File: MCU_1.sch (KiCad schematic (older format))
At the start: 18 parts, among them U2 STM32F051K6Ux

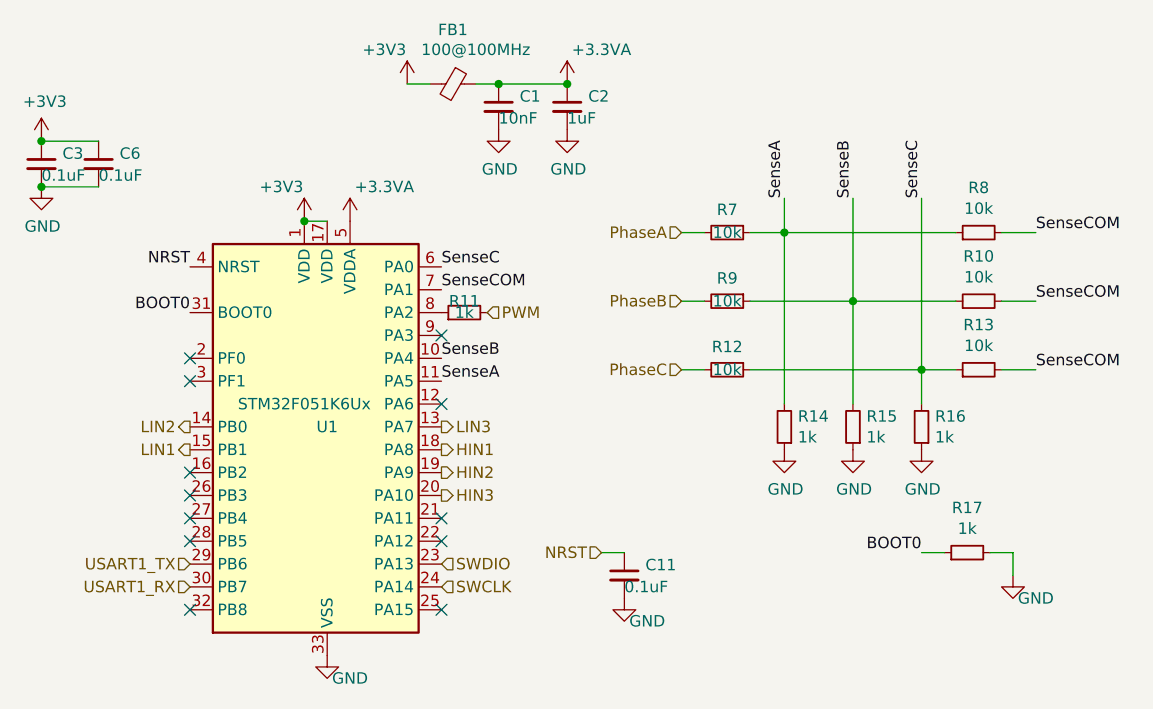
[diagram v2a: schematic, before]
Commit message: Rerouted a bunch of the phase traces so they are shorter
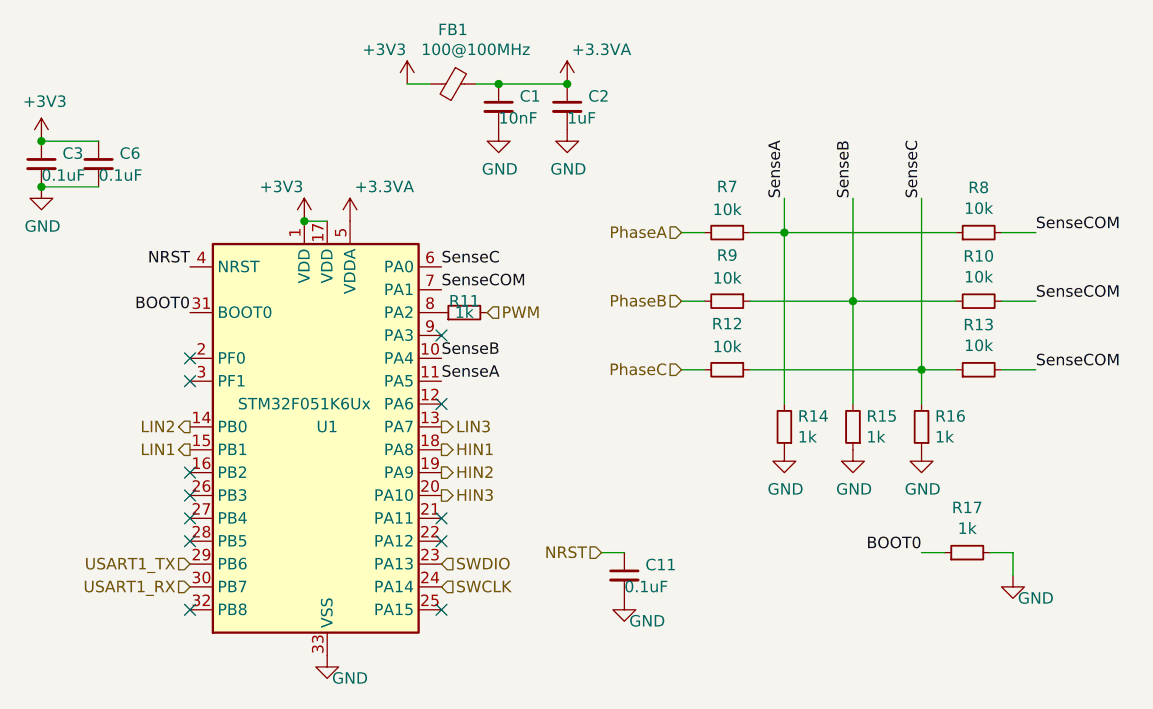
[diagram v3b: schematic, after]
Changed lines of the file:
@@
 AR Path="/6054D32F/6050F9A3" Ref="R7"  Part="1"
 AR Path="/605CA831/6050F9A3" Ref="R38"  Part="1"
-F 0 "R7" V 6700 2100 50  0000 C CNN
-F 1 "10k" V 6800 2100 50  0000 C CNN
+F 0 "R7" V 6600 2100 50  0000 C CNN
+F 1 "10k" V 6700 2100 50  0000 C CNN
 F 2 "Resistor_SMD:R_0402_1005Metric" H 6800 2100 50  0001 C CNN
 F 3 "~" H 6800 2100 50  0001 C CNN
@@
 AR Path="/6054D32F/6038A448" Ref="R9"  Part="1"
 AR Path="/605CA831/6038A448" Ref="R40"  Part="1"
-F 0 "R9" V 6700 2400 50  0000 C CNN
-F 1 "10k" V 6800 2400 50  0000 C CNN
+F 0 "R9" V 6600 2400 50  0000 C CNN
+F 1 "10k" V 6700 2400 50  0000 C CNN
 F 2 "Resistor_SMD:R_0402_1005Metric" H 6800 2400 50  0001 C CNN
 F 3 "~" H 6800 2400 50  0001 C CNN
@@
 AR Path="/6054D32F/6038D85A" Ref="R12"  Part="1"
 AR Path="/605CA831/6038D85A" Ref="R43"  Part="1"
-F 0 "R12" V 6700 2700 50  0000 C CNN
-F 1 "10k" V 6800 2700 50  0000 C CNN
+F 0 "R12" V 6600 2700 50  0000 C CNN
+F 1 "10k" V 6700 2700 50  0000 C CNN
 F 2 "Resistor_SMD:R_0402_1005Metric" H 6800 2700 50  0001 C CNN
 F 3 "~" H 6800 2700 50  0001 C CNN

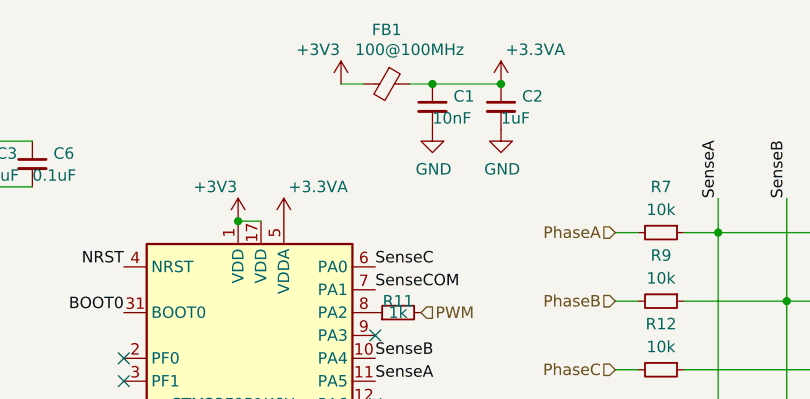
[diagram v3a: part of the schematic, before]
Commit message: Finished all traces and vias
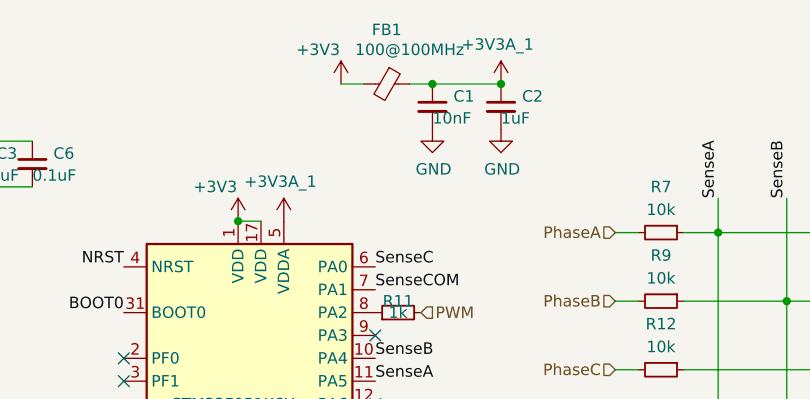
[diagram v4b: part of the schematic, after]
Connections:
- net +3.3VA renamed +3.3VA_1
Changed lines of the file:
@@
 NRST
-$Comp
-L power:+3.3VA #PWR0109
-U 1 1 604543F5
-P 5150 2050
-AR Path="/60302A40/604543F5" Ref="#PWR0109"  Part="1"
-AR Path="/605793E5/604543F5" Ref="#PWR?"  Part="1"
-AR Path="/6054D32F/604543F5" Ref="#PWR0127"  Part="1"
-AR Path="/605CA831/604543F5" Ref="#PWR0187"  Part="1"
-F 0 "#PWR0127" H 5150 1900 50  0001 C CNN
-F 1 "+3.3VA" H 5300 2200 50  0000 C CNN
-F 2 "" H 5150 2050 50  0001 C CNN
-F 3 "" H 5150 2050 50  0001 C CNN
-	1    5150 2050
-	1    0    0    -1
-$EndComp
 $Comp
 L power:+3V3 #PWR0110
@@
 F 3 "" H 5400 1450 50  0001 C CNN
 	1    5400 1450
-	1    0    0    -1
-$EndComp
-$Comp
-L power:+3.3VA #PWR0111
-U 1 1 6050F9B6
-P 6100 1450
-AR Path="/60302A40/6050F9B6" Ref="#PWR0111"  Part="1"
-AR Path="/605793E5/6050F9B6" Ref="#PWR?"  Part="1"
-AR Path="/6054D32F/6050F9B6" Ref="#PWR0162"  Part="1"
-AR Path="/605CA831/6050F9B6" Ref="#PWR0189"  Part="1"
-F 0 "#PWR0162" H 6100 1300 50  0001 C CNN
-F 1 "+3.3VA" H 6250 1600 50  0000 C CNN
-F 2 "" H 6100 1450 50  0001 C CNN
-F 3 "" H 6100 1450 50  0001 C CNN
-	1    6100 1450
 	1    0    0    -1
 $EndComp
@@
 Wire Wire Line
 	5700 1450 5800 1450
-Connection ~ 6100 1450
 Wire Wire Line
 	5800 1450 6100 1450
@@
 Text HLabel 4450 3550 0    50   Input ~ 0
 USART1_TX
+$Comp
+L power:+3V3A_1 #PWR0127
+U 1 1 6056120C
+P 5150 2050
+F 0 "#PWR0127" H 5150 1950 50  0001 C CNN
+F 1 "+3V3A_1" H 5135 2223 50  0000 C CNN
+F 2 "" H 5150 2050 50  0001 C CNN
+F 3 "" H 5150 2050 50  0001 C CNN
+	1    5150 2050
+	1    0    0    -1
+$EndComp
+$Comp
+L power:+3V3A_1 #PWR?
+U 1 1 6056DE0B
+P 6100 1450
+F 0 "#PWR?" H 6100 1350 50  0001 C CNN
+F 1 "+3V3A_1" H 6085 1623 50  0000 C CNN
+F 2 "" H 6100 1450 50  0001 C CNN
+F 3 "" H 6100 1450 50  0001 C CNN
+	1    6100 1450
+	1    0    0    -1
+$EndComp
+Connection ~ 6100 1450
 $EndSCHEMATC

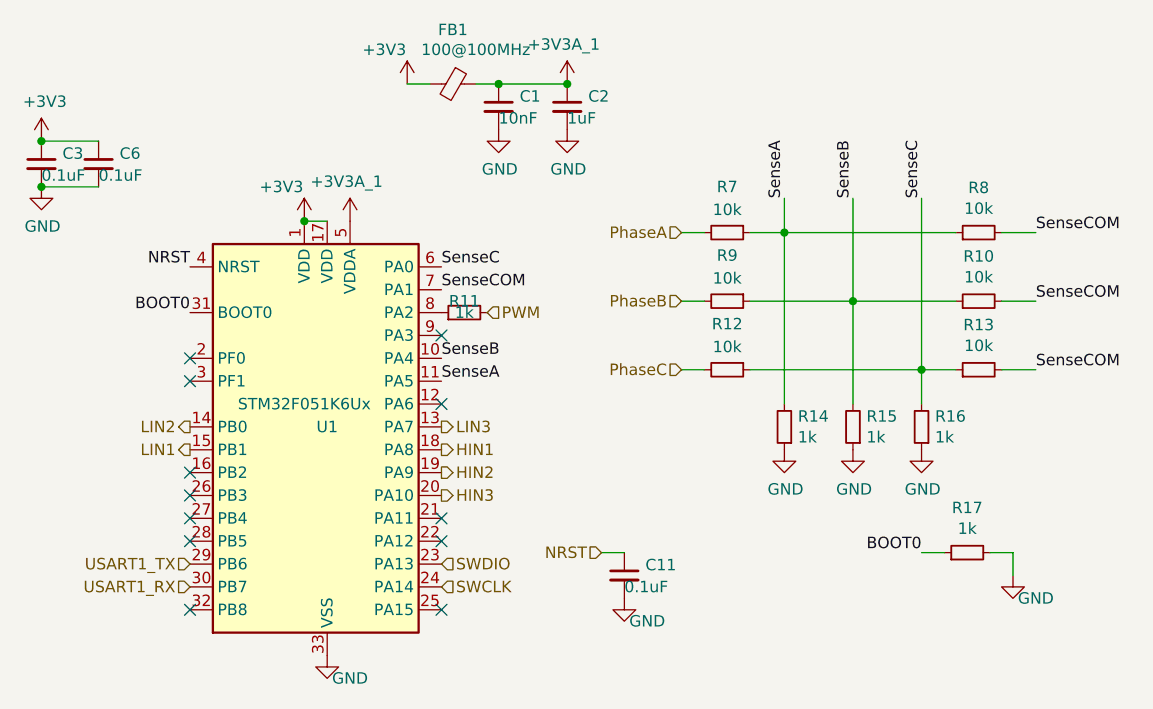
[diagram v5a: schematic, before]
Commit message: Changed shunt resistor footprint and changed edge cuts to accomodate larger size
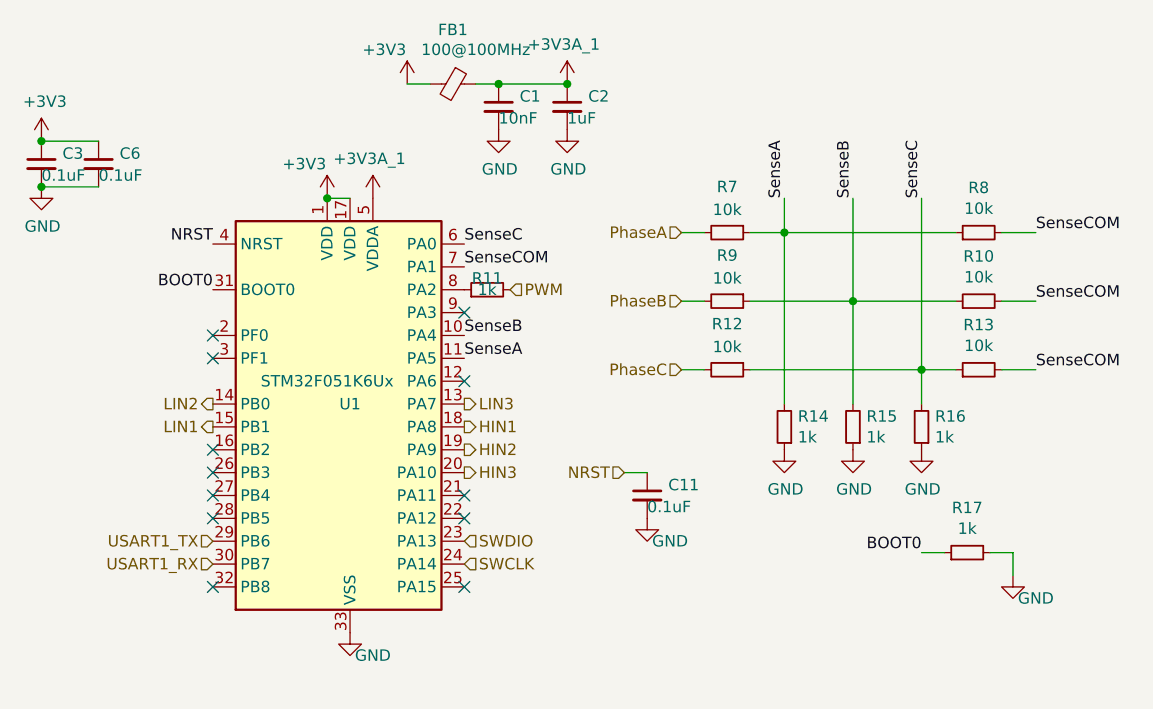
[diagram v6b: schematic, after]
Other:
- moved on the sheet: C11, R11, U1
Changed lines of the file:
@@
 L MCU_ST_STM32F0:STM32F051K6Ux U2
 U 1 1 60305B87
-P 5050 2950
+P 5150 2850
 AR Path="/60302A40/60305B87" Ref="U2"  Part="1"
 AR Path="/605793E5/60305B87" Ref="U?"  Part="1"
 AR Path="/6054D32F/60305B87" Ref="U1"  Part="1"
 AR Path="/605CA831/60305B87" Ref="U9"  Part="1"
-F 0 "U1" H 5050 2950 50  0000 C CNN
-F 1 "STM32F051K6Ux" H 4950 3050 50  0000 C CNN
-F 2 "Package_DFN_QFN:QFN-32-1EP_5x5mm_P0.5mm_EP3.45x3.45mm" H 4550 2050 50  0001 R CNN
-F 3 "http://www.st.com/st-web-ui/static/active/en/resource/technical/document/datasheet/DM00039193.pdf" H 5050 2950 50  0001 C CNN
-	1    5050 2950
+F 0 "U1" H 5150 2850 50  0000 C CNN
+F 1 "STM32F051K6Ux" H 5050 2950 50  0000 C CNN
+F 2 "Package_DFN_QFN:QFN-32-1EP_5x5mm_P0.5mm_EP3.45x3.45mm" H 4650 1950 50  0001 R CNN
+F 3 "http://www.st.com/st-web-ui/static/active/en/resource/technical/document/datasheet/DM00039193.pdf" H 5150 2850 50  0001 C CNN
+	1    5150 2850
 	1    0    0    -1
 $EndComp
@@
 L power:+3V3 #PWR020
 U 1 1 60305B8D
-P 4950 2050
+P 5050 1950
 AR Path="/60302A40/60305B8D" Ref="#PWR020"  Part="1"
 AR Path="/605793E5/60305B8D" Ref="#PWR?"  Part="1"
 AR Path="/6054D32F/60305B8D" Ref="#PWR0109"  Part="1"
 AR Path="/605CA831/60305B8D" Ref="#PWR0178"  Part="1"
-F 0 "#PWR0109" H 4950 1900 50  0001 C CNN
-F 1 "+3V3" H 4850 2200 50  0000 C CNN
-F 2 "" H 4950 2050 50  0001 C CNN
-F 3 "" H 4950 2050 50  0001 C CNN
-	1    4950 2050
+F 0 "#PWR0109" H 5050 1800 50  0001 C CNN
+F 1 "+3V3" H 4950 2100 50  0000 C CNN
+F 2 "" H 5050 1950 50  0001 C CNN
+F 3 "" H 5050 1950 50  0001 C CNN
+	1    5050 1950
 	1    0    0    -1
 $EndComp
 Wire Wire Line
-	4950 2050 5050 2050
-Connection ~ 4950 2050
+	5050 1950 5150 1950
+Connection ~ 5050 1950
 $Comp
 L power:GND #PWR021
 U 1 1 6050F99D
-P 5050 3950
+P 5150 3850
 AR Path="/60302A40/6050F99D" Ref="#PWR021"  Part="1"
 AR Path="/605793E5/6050F99D" Ref="#PWR?"  Part="1"
 AR Path="/6054D32F/6050F99D" Ref="#PWR0110"  Part="1"
 AR Path="/605CA831/6050F99D" Ref="#PWR0179"  Part="1"
-F 0 "#PWR0110" H 5050 3700 50  0001 C CNN
-F 1 "GND" H 5150 3850 50  0000 C CNN
-F 2 "" H 5050 3950 50  0001 C CNN
-F 3 "" H 5050 3950 50  0001 C CNN
-	1    5050 3950
+F 0 "#PWR0110" H 5150 3600 50  0001 C CNN
+F 1 "GND" H 5250 3750 50  0000 C CNN
+F 2 "" H 5150 3850 50  0001 C CNN
+F 3 "" H 5150 3850 50  0001 C CNN
+	1    5150 3850
 	1    0    0    -1
 $EndComp
@@
 	1    0    0    -1
 $EndComp
-Text HLabel 4450 3050 0    50   Output ~ 0
+Text HLabel 4550 2950 0    50   Output ~ 0
 LIN1
-Text HLabel 4450 2950 0    50   Output ~ 0
+Text HLabel 4550 2850 0    50   Output ~ 0
 LIN2
-Text HLabel 5550 2950 2    50   Output ~ 0
+Text HLabel 5650 2850 2    50   Output ~ 0
 LIN3
-Text HLabel 5550 3250 2    50   Output ~ 0
+Text HLabel 5650 3150 2    50   Output ~ 0
 HIN3
-Text HLabel 5550 3150 2    50   Output ~ 0
+Text HLabel 5650 3050 2    50   Output ~ 0
 HIN2
-Text HLabel 5550 3050 2    50   Output ~ 0
+Text HLabel 5650 2950 2    50   Output ~ 0
 HIN1
 Text HLabel 6600 2100 0    50   Input ~ 0
@@
 Text Label 8150 2100 0    50   ~ 0
 SenseCOM
-Text Label 5550 2750 0    50   ~ 0
+Text Label 5650 2650 0    50   ~ 0
 SenseA
-Text Label 5550 2650 0    50   ~ 0
+Text Label 5650 2550 0    50   ~ 0
 SenseB
-Text Label 5550 2250 0    50   ~ 0
+Text Label 5650 2150 0    50   ~ 0
 SenseC
-Text Label 5550 2350 0    50   ~ 0
+Text Label 5650 2250 0    50   ~ 0
 SenseCOM
 Text Label 7050 1950 1    50   ~ 0
@@
 Wire Wire Line
 	7800 2100 7050 2100
-Text Label 4450 2250 2    50   ~ 0
+Text Label 4550 2150 2    50   ~ 0
 NRST
 $Comp
 L power:GND #PWR010
 U 1 1 6039EC90
-P 6350 3700
+P 6450 3350
 AR Path="/60302A40/6039EC90" Ref="#PWR010"  Part="1"
 AR Path="/605793E5/6039EC90" Ref="#PWR?"  Part="1"
 AR Path="/6054D32F/6039EC90" Ref="#PWR0125"  Part="1"
 AR Path="/605CA831/6039EC90" Ref="#PWR0185"  Part="1"
-F 0 "#PWR0125" H 6350 3450 50  0001 C CNN
-F 1 "GND" H 6450 3600 50  0000 C CNN
-F 2 "" H 6350 3700 50  0001 C CNN
-F 3 "" H 6350 3700 50  0001 C CNN
-	1    6350 3700
+F 0 "#PWR0125" H 6450 3100 50  0001 C CNN
+F 1 "GND" H 6550 3250 50  0000 C CNN
+F 2 "" H 6450 3350 50  0001 C CNN
+F 3 "" H 6450 3350 50  0001 C CNN
+	1    6450 3350
 	1    0    0    -1
 $EndComp
 Wire Wire Line
-	6250 3500 6350 3500
-Text Label 4450 2450 2    50   ~ 0
+	6350 3150 6450 3150
+Text Label 4550 2350 2    50   ~ 0
 BOOT0
 Text Label 7650 3500 2    50   ~ 0
@@
 Wire Wire Line
 	8050 3500 7950 3500
-Text HLabel 5750 2450 2    50   Input ~ 0
+Text HLabel 5850 2350 2    50   Input ~ 0
 PWM
 $Comp
 L Device:R_Small R24
 U 1 1 603A2EC9
-P 5650 2450
+P 5750 2350
 AR Path="/60302A40/603A2EC9" Ref="R24"  Part="1"
 AR Path="/605793E5/603A2EC9" Ref="R?"  Part="1"
 AR Path="/6054D32F/603A2EC9" Ref="R11"  Part="1"
 AR Path="/605CA831/603A2EC9" Ref="R42"  Part="1"
-F 0 "R11" V 5700 2450 50  0000 C CNN
-F 1 "1k" V 5650 2450 50  0000 C CNN
-F 2 "Resistor_SMD:R_0402_1005Metric" H 5650 2450 50  0001 C CNN
-F 3 "~" H 5650 2450 50  0001 C CNN
-	1    5650 2450
+F 0 "R11" V 5800 2350 50  0000 C CNN
+F 1 "1k" V 5750 2350 50  0000 C CNN
+F 2 "Resistor_SMD:R_0402_1005Metric" H 5750 2350 50  0001 C CNN
+F 3 "~" H 5750 2350 50  0001 C CNN
+	1    5750 2350
 	0    -1   -1   0
 $EndComp
-NoConn ~ 5550 2550
-NoConn ~ 5550 2850
-NoConn ~ 5550 3450
-NoConn ~ 5550 3350
-NoConn ~ 5550 3750
-NoConn ~ 4450 3750
-NoConn ~ 4450 3450
-NoConn ~ 4450 3350
-NoConn ~ 4450 3250
-NoConn ~ 4450 3150
-NoConn ~ 4450 2650
-NoConn ~ 4450 2750
+NoConn ~ 5650 2450
+NoConn ~ 5650 2750
+NoConn ~ 5650 3350
+NoConn ~ 5650 3250
+NoConn ~ 5650 3650
+NoConn ~ 4550 3650
+NoConn ~ 4550 3350
+NoConn ~ 4550 3250
+NoConn ~ 4550 3150
+NoConn ~ 4550 3050
+NoConn ~ 4550 2550
+NoConn ~ 4550 2650
 $Comp
 L Device:C_Small C?
 U 1 1 603AA2FF
-P 6350 3600
+P 6450 3250
 AR Path="/603AA2FF" Ref="C?"  Part="1"
 AR Path="/60302A40/603AA2FF" Ref="C15"  Part="1"
@@
 AR Path="/6054D32F/603AA2FF" Ref="C11"  Part="1"
 AR Path="/605CA831/603AA2FF" Ref="C36"  Part="1"
-F 0 "C11" H 6442 3646 50  0000 L CNN
-F 1 "0.1uF" H 6350 3550 50  0000 L CNN
-F 2 "Capacitor_SMD:C_0402_1005Metric" H 6350 3600 50  0001 C CNN
-F 3 "~" H 6350 3600 50  0001 C CNN
-	1    6350 3600
+F 0 "C11" H 6542 3296 50  0000 L CNN
+F 1 "0.1uF" H 6450 3200 50  0000 L CNN
+F 2 "Capacitor_SMD:C_0402_1005Metric" H 6450 3250 50  0001 C CNN
+F 3 "~" H 6450 3250 50  0001 C CNN
+	1    6450 3250
 	1    0    0    -1
 $EndComp
-Text HLabel 5550 3550 2    50   Input ~ 0
+Text HLabel 5650 3450 2    50   Input ~ 0
 SWDIO
-Text HLabel 5550 3650 2    50   Input ~ 0
+Text HLabel 5650 3550 2    50   Input ~ 0
 SWCLK
 $Bitmap
-Pos 2650 3150
+Pos 2750 3150
 Scale 1.000000
 Data
@@
 Wire Wire Line
 	7050 2100 7050 2850
-Text HLabel 6250 3500 0    50   Input ~ 0
+Text HLabel 6350 3150 0    50   Input ~ 0
 NRST
 $Comp
@@
 	1    0    0    -1
 $EndComp
-Text HLabel 4450 3650 0    50   Input ~ 0
+Text HLabel 4550 3550 0    50   Input ~ 0
 USART1_RX
-Text HLabel 4450 3550 0    50   Input ~ 0
+Text HLabel 4550 3450 0    50   Input ~ 0
 USART1_TX
 $Comp
 L power:+3V3A_1 #PWR0127
 U 1 1 6056120C
-P 5150 2050
-F 0 "#PWR0127" H 5150 1950 50  0001 C CNN
-F 1 "+3V3A_1" H 5135 2223 50  0000 C CNN
-F 2 "" H 5150 2050 50  0001 C CNN
-F 3 "" H 5150 2050 50  0001 C CNN
-	1    5150 2050
+P 5250 1950
+F 0 "#PWR0127" H 5250 1850 50  0001 C CNN
+F 1 "+3V3A_1" H 5235 2123 50  0000 C CNN
+F 2 "" H 5250 1950 50  0001 C CNN
+F 3 "" H 5250 1950 50  0001 C CNN
+	1    5250 1950
 	1    0    0    -1
 $EndComp
